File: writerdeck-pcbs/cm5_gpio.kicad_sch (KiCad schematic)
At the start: 1 part

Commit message: power management done
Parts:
- added D2: Red LED, LED_SMD:LED_0805_2012Metric, symbol ZF_common:0805 Red LED
- added D3: Green LED, LED_SMD:LED_0805_2012Metric, symbol ZF_common:0805 Green LED
- added R15, R16: 1k, Resistor_SMD:R_0603_1608Metric, symbol ZF_common:1k 1% 0603 Resistor
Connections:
- net LED_nACT: now reaches Module1.21 (LED_nACT)
- net LED_nACT: now also R16.2
- net PWR_BUT: now reaches Module1.92 (PWR_BUT)
- net LED_nPWR: now reaches Module1.95 (LED_nPWR)
- net LED_nPWR: now also R15.2
- new net: D2.1 (K), R15.1
- new net: D3.1 (K), R16.1
- new net +3V3: D2.2 (A), D3.2 (A)
- no-connect marks 0 -> 11
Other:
- moved on the sheet: Module1A

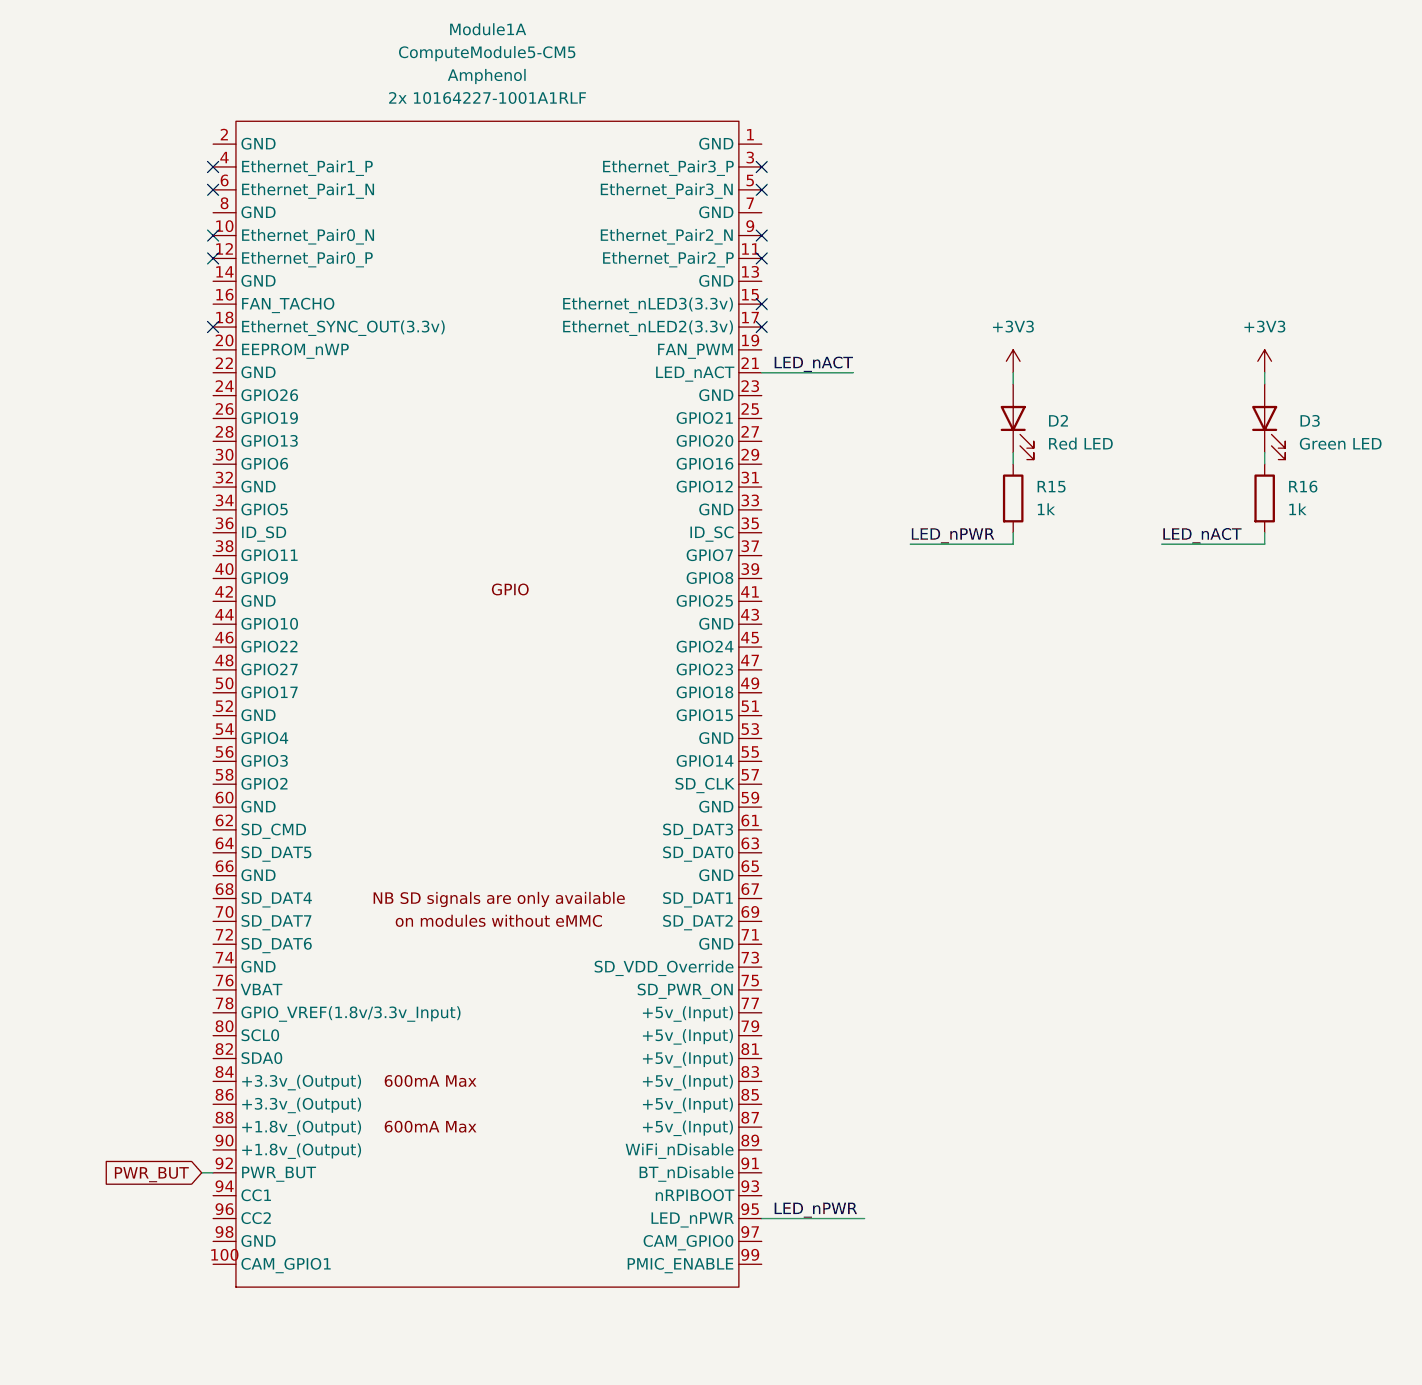
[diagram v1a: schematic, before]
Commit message: pre switch matrix, restructure
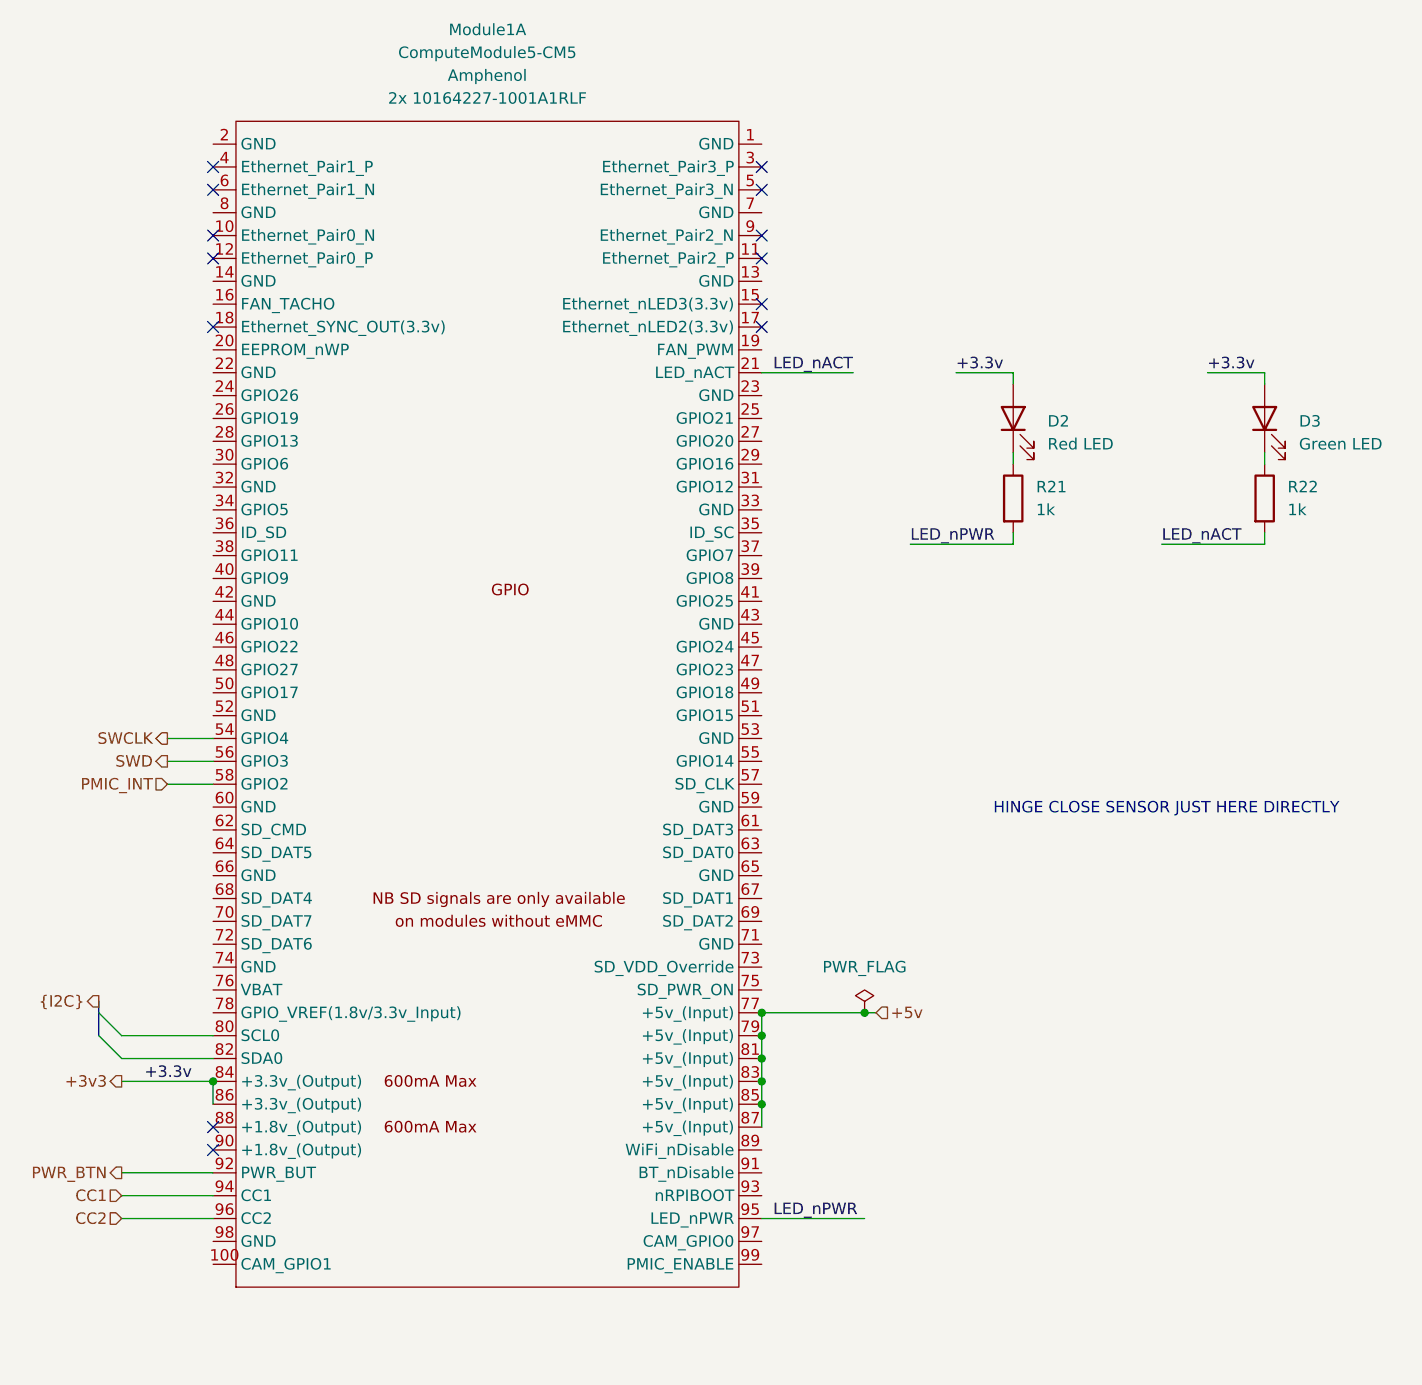
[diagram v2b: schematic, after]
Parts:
- renumbered R15 to R21, R16 to R22
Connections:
- net +3V3 is gone; now on net +3v3: D2.2 (A), D3.2 (A)
- net SWCLK: now reaches Module1.54 (GPIO4)
- net SWD: now reaches Module1.56 (GPIO3)
- net PMIC_INT: now reaches Module1.58 (GPIO2)
- net +5v: now reaches Module1.77 (+5v_(Input))
- net +5v: now also Module1.79 (+5v_(Input)), Module1.81 (+5v_(Input)), Module1.83 (+5v_(Input)), Module1.85 (+5v_(Input)), Module1.87 (+5v_(Input))
- net +3v3: now reaches Module1.84 (+3.3v_(Output))
- net +3v3: now also Module1.86 (+3.3v_(Output))
- net CC1: now reaches Module1.94 (CC1)
- net CC2: now reaches Module1.96 (CC2)
- net PWR_BUT renamed PWR_BTN
- no-connect marks 11 -> 13
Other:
- note added: "HINGE CLOSE SENSOR JUST HERE DIRECTLY"

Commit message: backup
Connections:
- net +3v3: now also Module1.78 (GPIO_VREF(1.8v/3.3v_Input))
- no-connect marks 13 -> 14
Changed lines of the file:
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@@
+	)
+	(no_connect
+		(at 99.06 152.4)
 	)
 	(no_connect
@@
 		(pts
 			(xy 33.02 99.06) (xy 38.1 99.06)
+		)
+		(stroke
+			(width 0)
+			(type default)
+		)
+	)
+	(wire
+		(pts
+			(xy 30.48 124.46) (xy 38.1 124.46)
 		)
 		(stroke
@@
 		(effects
 			(font
+				(size 1.27 1.27)
+			)
+			(justify left bottom)
+		)
+	)
+	(label "+3.3v"
+		(at 30.48 124.46 0)
+		(effects
+			(font
